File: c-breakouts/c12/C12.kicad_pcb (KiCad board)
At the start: 2 copper layers, 38.1 x 48.3 mm, 14 parts, among them J0 Conn_01x01_Male, J1 Conn_01x01_Male, J2 Conn_01x01_Male, J3 Conn_01x01_Male, J4 Conn_01x08_Female, J5 Conn_01x08_Female, J6 Conn_01x08_Female, J7 Conn_01x08_Female

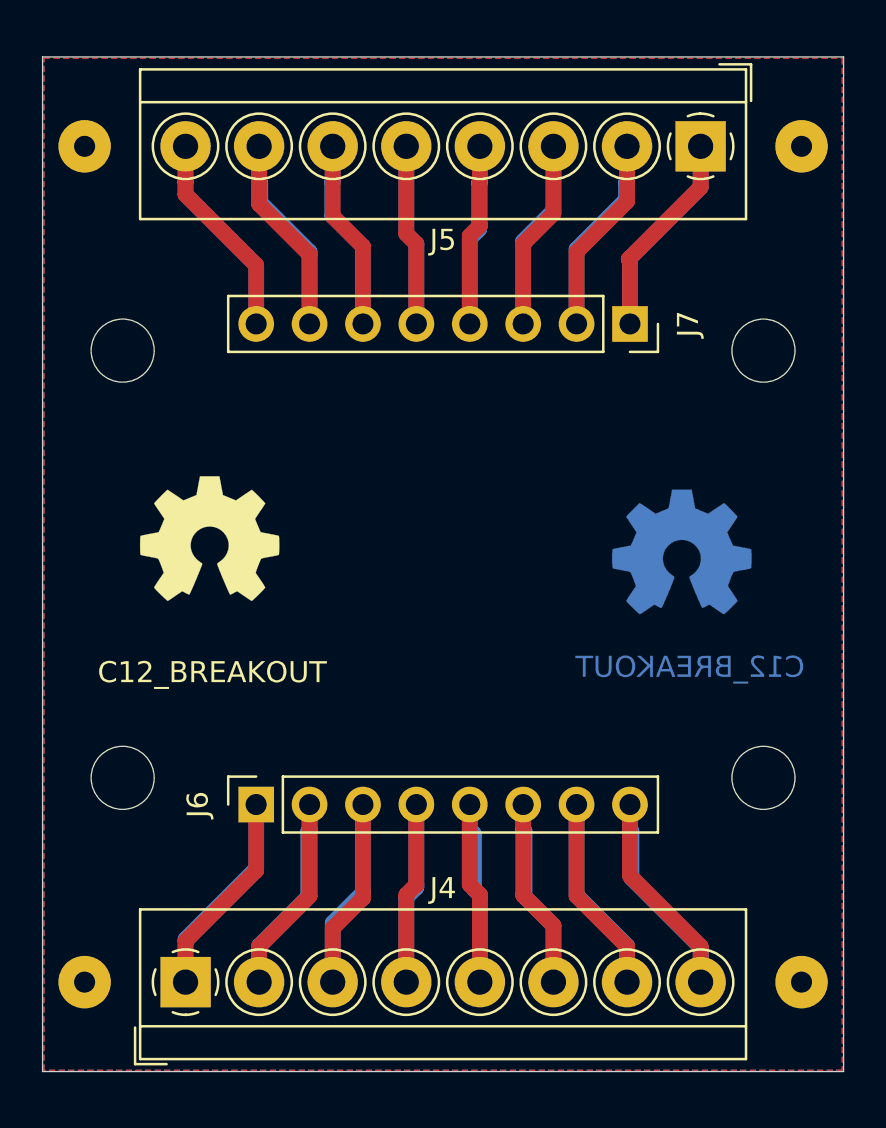
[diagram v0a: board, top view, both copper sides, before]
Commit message: expanded breakout C012 to wemos esp32
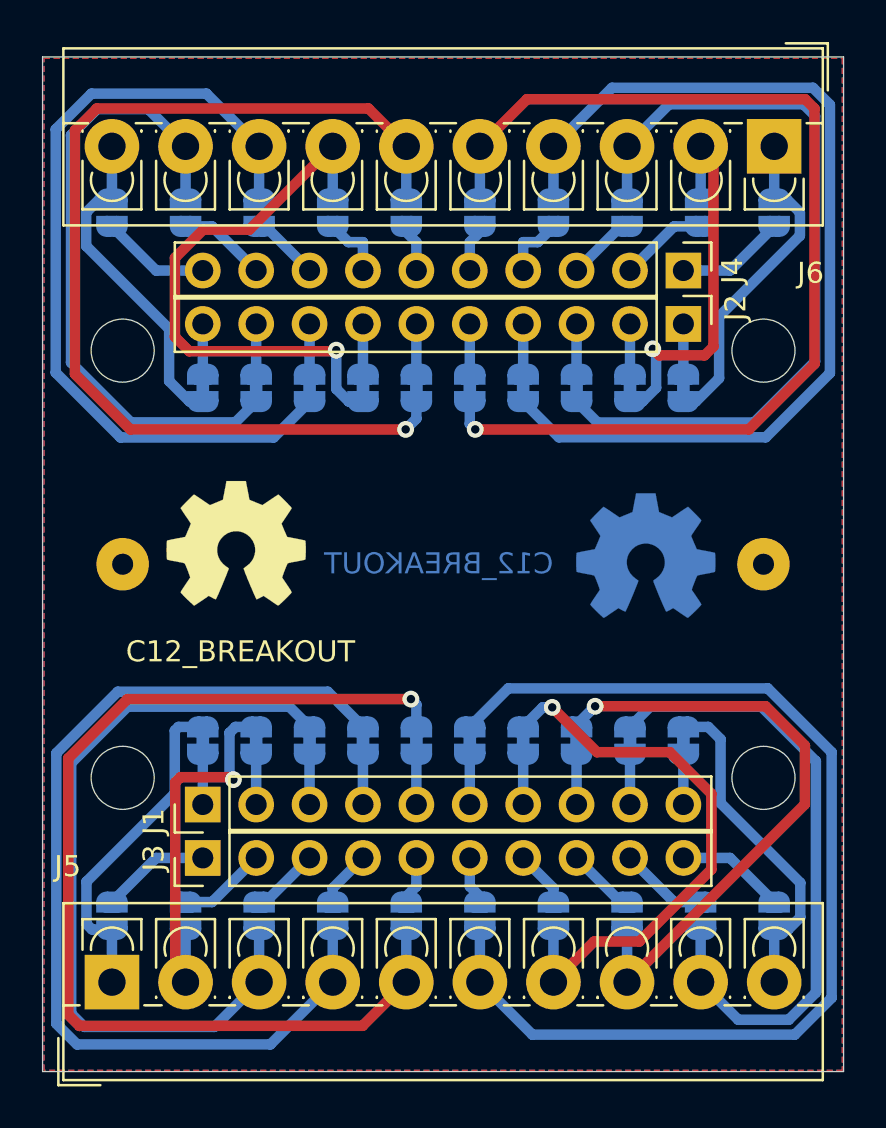
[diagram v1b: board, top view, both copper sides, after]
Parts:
- removed J7: Conn_01x08_Female, Connector_PinSocket_2.54mm:PinSocket_1x08_P2.54mm_Vertical
- added J1: Conn_01x10_Female, Connector_PinHeader_2.54mm:PinHeader_1x10_P2.54mm_Vertical, F.Cu at (27.6, 55.6)
- added JP1: SolderJumper_2_Bridged, Jumper:SolderJumper-2_P1.3mm_Bridged_RoundedPad1.0x1.5mm, B.Cu at (27.6, 52.5)
- added JP10: SolderJumper_2_Bridged, Jumper:SolderJumper-2_P1.3mm_Bridged_RoundedPad1.0x1.5mm, B.Cu at (50.5, 52.5)
- added JP11: SolderJumper_2_Open, Jumper:SolderJumper-2_P1.3mm_Open_RoundedPad1.0x1.5mm, B.Cu at (23.3, 60.9)
- added JP12: SolderJumper_2_Open, Jumper:SolderJumper-2_P1.3mm_Open_RoundedPad1.0x1.5mm, B.Cu at (26.8, 60.9)
- added JP13: SolderJumper_2_Open, Jumper:SolderJumper-2_P1.3mm_Open_RoundedPad1.0x1.5mm, B.Cu at (30.3, 60.9)
- added JP14: SolderJumper_2_Open, Jumper:SolderJumper-2_P1.3mm_Open_RoundedPad1.0x1.5mm, B.Cu at (33.8, 60.9)
- added JP15: SolderJumper_2_Open, Jumper:SolderJumper-2_P1.3mm_Open_RoundedPad1.0x1.5mm, B.Cu at (37.3, 60.9)
- added JP16: SolderJumper_2_Open, Jumper:SolderJumper-2_P1.3mm_Open_RoundedPad1.0x1.5mm, B.Cu at (40.8, 60.9)
- added JP17: SolderJumper_2_Open, Jumper:SolderJumper-2_P1.3mm_Open_RoundedPad1.0x1.5mm, B.Cu at (44.3, 60.9)
- added JP18: SolderJumper_2_Open, Jumper:SolderJumper-2_P1.3mm_Open_RoundedPad1.0x1.5mm, B.Cu at (47.8, 60.9)
- added JP19: SolderJumper_2_Open, Jumper:SolderJumper-2_P1.3mm_Open_RoundedPad1.0x1.5mm, B.Cu at (51.3, 60.9)
- added JP2: SolderJumper_2_Bridged, Jumper:SolderJumper-2_P1.3mm_Bridged_RoundedPad1.0x1.5mm, B.Cu at (30.2, 52.5)
- added JP20: SolderJumper_2_Open, Jumper:SolderJumper-2_P1.3mm_Open_RoundedPad1.0x1.5mm, B.Cu at (54.8, 60.9)
- added JP21: SolderJumper_2_Bridged, Jumper:SolderJumper-2_P1.3mm_Bridged_RoundedPad1.0x1.5mm, B.Cu at (50.5, 35.7)
- added JP22: SolderJumper_2_Bridged, Jumper:SolderJumper-2_P1.3mm_Bridged_RoundedPad1.0x1.5mm, B.Cu at (47.9, 35.7)
- added JP23: SolderJumper_2_Bridged, Jumper:SolderJumper-2_P1.3mm_Bridged_RoundedPad1.0x1.5mm, B.Cu at (45.4, 35.7)
- added JP24: SolderJumper_2_Bridged, Jumper:SolderJumper-2_P1.3mm_Bridged_RoundedPad1.0x1.5mm, B.Cu at (42.9, 35.7)
- added JP25: SolderJumper_2_Bridged, Jumper:SolderJumper-2_P1.3mm_Bridged_RoundedPad1.0x1.5mm, B.Cu at (40.3, 35.7)
- added JP26: SolderJumper_2_Bridged, Jumper:SolderJumper-2_P1.3mm_Bridged_RoundedPad1.0x1.5mm, B.Cu at (37.8, 35.7)
- added JP27: SolderJumper_2_Bridged, Jumper:SolderJumper-2_P1.3mm_Bridged_RoundedPad1.0x1.5mm, B.Cu at (35.2, 35.7)
- added JP28: SolderJumper_2_Bridged, Jumper:SolderJumper-2_P1.3mm_Bridged_RoundedPad1.0x1.5mm, B.Cu at (32.7, 35.7)
- added JP29: SolderJumper_2_Bridged, Jumper:SolderJumper-2_P1.3mm_Bridged_RoundedPad1.0x1.5mm, B.Cu at (30.2, 35.7)
- added JP3: SolderJumper_2_Bridged, Jumper:SolderJumper-2_P1.3mm_Bridged_RoundedPad1.0x1.5mm, B.Cu at (32.7, 52.5)
- added JP30: SolderJumper_2_Bridged, Jumper:SolderJumper-2_P1.3mm_Bridged_RoundedPad1.0x1.5mm, B.Cu at (27.6, 35.7)
- added JP31: SolderJumper_2_Open, Jumper:SolderJumper-2_P1.3mm_Open_RoundedPad1.0x1.5mm, B.Cu at (54.8, 27.4)
- added JP32: SolderJumper_2_Open, Jumper:SolderJumper-2_P1.3mm_Open_RoundedPad1.0x1.5mm, B.Cu at (51.3, 27.4)
- added JP33: SolderJumper_2_Open, Jumper:SolderJumper-2_P1.3mm_Open_RoundedPad1.0x1.5mm, B.Cu at (47.8, 27.4)
- added JP34: SolderJumper_2_Open, Jumper:SolderJumper-2_P1.3mm_Open_RoundedPad1.0x1.5mm, B.Cu at (44.3, 27.4)
- added JP35: SolderJumper_2_Open, Jumper:SolderJumper-2_P1.3mm_Open_RoundedPad1.0x1.5mm, B.Cu at (40.8, 27.4)
- added JP36: SolderJumper_2_Open, Jumper:SolderJumper-2_P1.3mm_Open_RoundedPad1.0x1.5mm, B.Cu at (37.3, 27.4)
- added JP37: SolderJumper_2_Open, Jumper:SolderJumper-2_P1.3mm_Open_RoundedPad1.0x1.5mm, B.Cu at (33.8, 27.4)
- added JP38: SolderJumper_2_Open, Jumper:SolderJumper-2_P1.3mm_Open_RoundedPad1.0x1.5mm, B.Cu at (30.3, 27.4)
- added JP39: SolderJumper_2_Open, Jumper:SolderJumper-2_P1.3mm_Open_RoundedPad1.0x1.5mm, B.Cu at (26.8, 27.4)
- added JP4: SolderJumper_2_Bridged, Jumper:SolderJumper-2_P1.3mm_Bridged_RoundedPad1.0x1.5mm, B.Cu at (35.2, 52.5)
- added JP40: SolderJumper_2_Open, Jumper:SolderJumper-2_P1.3mm_Open_RoundedPad1.0x1.5mm, B.Cu at (23.3, 27.4)
- added JP5: SolderJumper_2_Bridged, Jumper:SolderJumper-2_P1.3mm_Bridged_RoundedPad1.0x1.5mm, B.Cu at (37.8, 52.5)
- added JP6: SolderJumper_2_Bridged, Jumper:SolderJumper-2_P1.3mm_Bridged_RoundedPad1.0x1.5mm, B.Cu at (40.3, 52.5)
- added JP7: SolderJumper_2_Bridged, Jumper:SolderJumper-2_P1.3mm_Bridged_RoundedPad1.0x1.5mm, B.Cu at (42.9, 52.5)
- added JP8: SolderJumper_2_Bridged, Jumper:SolderJumper-2_P1.3mm_Bridged_RoundedPad1.0x1.5mm, B.Cu at (45.4, 52.5)
- added JP9: SolderJumper_2_Bridged, Jumper:SolderJumper-2_P1.3mm_Bridged_RoundedPad1.0x1.5mm, B.Cu at (47.9, 52.5)
- J2, J3: value Conn_01x01_Male -> Conn_01x10_Female; footprint Connector_Wire:SolderWirePad_1x01_Drill1mm -> Connector_PinHeader_2.54mm:PinHeader_1x10_P2.54mm_Vertical
- J4: value Conn_01x08_Female -> Conn_01x10_Female; footprint TerminalBlock_4Ucon:TerminalBlock_4Ucon_1x08_P3.50mm_Horizontal -> Connector_PinHeader_2.54mm:PinHeader_1x10_P2.54mm_Vertical
- J5: value Conn_01x08_Female -> Conn_01x10_Female; footprint TerminalBlock_4Ucon:TerminalBlock_4Ucon_1x08_P3.50mm_Horizontal -> TerminalBlock_4Ucon:TerminalBlock_4Ucon_1x10_P3.50mm_Vertical
- J6: value Conn_01x08_Female -> Conn_01x10_Female; footprint Connector_PinSocket_2.54mm:PinSocket_1x08_P2.54mm_Vertical -> TerminalBlock_4Ucon:TerminalBlock_4Ucon_1x10_P3.50mm_Vertical
- moved J5 48.6 mm to (23.3, 64.0), turned to 0 degrees
- moved J3 44.2 mm to (27.6, 58.1), turned to 90 degrees
- moved J4 41.3 mm to (50.5, 30.2), turned to 270 degrees
- moved J6 39.8 mm to (54.8, 24.3), turned to 180 degrees
- moved J11 37.9 mm to (54.3, 44.1)
- moved J2 31.8 mm to (50.5, 32.7), turned to 270 degrees
- moved J10 20.0 mm to (23.8, 44.1)
- moved REFS0** 1.73 mm to (48.7, 43.7)
- moved REFS1** 1.28 mm to (29.2, 43.1)
- renumbered J0 to J10, J1 to J11, REF** to REFS0**, REF** to REFS1**
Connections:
- J10 pad 1: Net-(J0-Pad1) -> Net-(J10-Pad1)
- J11 pad 1: Net-(J0-Pad1) -> Net-(J10-Pad1)
- J2 pad 1: Net-(J0-Pad1) -> Net-(J2-Pad1)
- J3 pad 1: Net-(J0-Pad1) -> Net-(J3-Pad1)
- J6 pad 1: Net-(J4-Pad1) -> Net-(J6-Pad1)
- J6 pad 2: Net-(J4-Pad2) -> Net-(J6-Pad2)
- J6 pad 3: Net-(J4-Pad3) -> Net-(J6-Pad3)
- J6 pad 4: Net-(J4-Pad4) -> Net-(J6-Pad4)
- J6 pad 5: Net-(J4-Pad5) -> Net-(J6-Pad5)
- J6 pad 6: Net-(J4-Pad6) -> Net-(J6-Pad6)
- J6 pad 7: Net-(J4-Pad7) -> Net-(J6-Pad7)
- J6 pad 8: Net-(J4-Pad8) -> Net-(J6-Pad8)
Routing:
- net Net-(J6-Pad5): track 0.00 -> 50.5 mm, vias 0 -> 1
- net Net-(J6-Pad6): track 0.00 -> 49.4 mm, vias 0 -> 1
- net Net-(J6-Pad4): track 0.00 -> 46.5 mm
- net Net-(J6-Pad8): track 0.00 -> 39.6 mm
- net Net-(J6-Pad3): track 0.00 -> 37.2 mm
- net Net-(J5-Pad6): track 18.1 -> 51.9 mm
- net Net-(J5-Pad5): track 17.3 -> 50.8 mm, vias 0 -> 1
- net Net-(J5-Pad9): track 0.00 -> 30.6 mm
- net Net-(J6-Pad9): track 0.00 -> 30.4 mm
- net Net-(J5-Pad4): track 17.3 -> 46.6 mm
- net Net-(J6-Pad7): track 0.00 -> 27.3 mm, vias 0 -> 1
- net Net-(J5-Pad3): track 18.1 -> 37.4 mm
- net Net-(J6-Pad2): track 0.00 -> 18.9 mm, vias 0 -> 1
- net Net-(J4-Pad8): track 19.7 -> 3.27 mm
- net Net-(J5-Pad10): track 0.00 -> 16.0 mm
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- added copper zone on B.Cu, net Net-(J10-Pad1)
- added copper zone on F.Cu, net Net-(J10-Pad1)
- removed copper zone on B.Cu, net Net-(J0-Pad1)
- removed copper zone on F.Cu, net Net-(J0-Pad1)
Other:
- net class Default: trace_width 0.75 -> 0.5
